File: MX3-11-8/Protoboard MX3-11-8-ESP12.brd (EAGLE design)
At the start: 74 x 99.4 mm, 638 parts, among them J1 DCJ0202, X3 RJ45

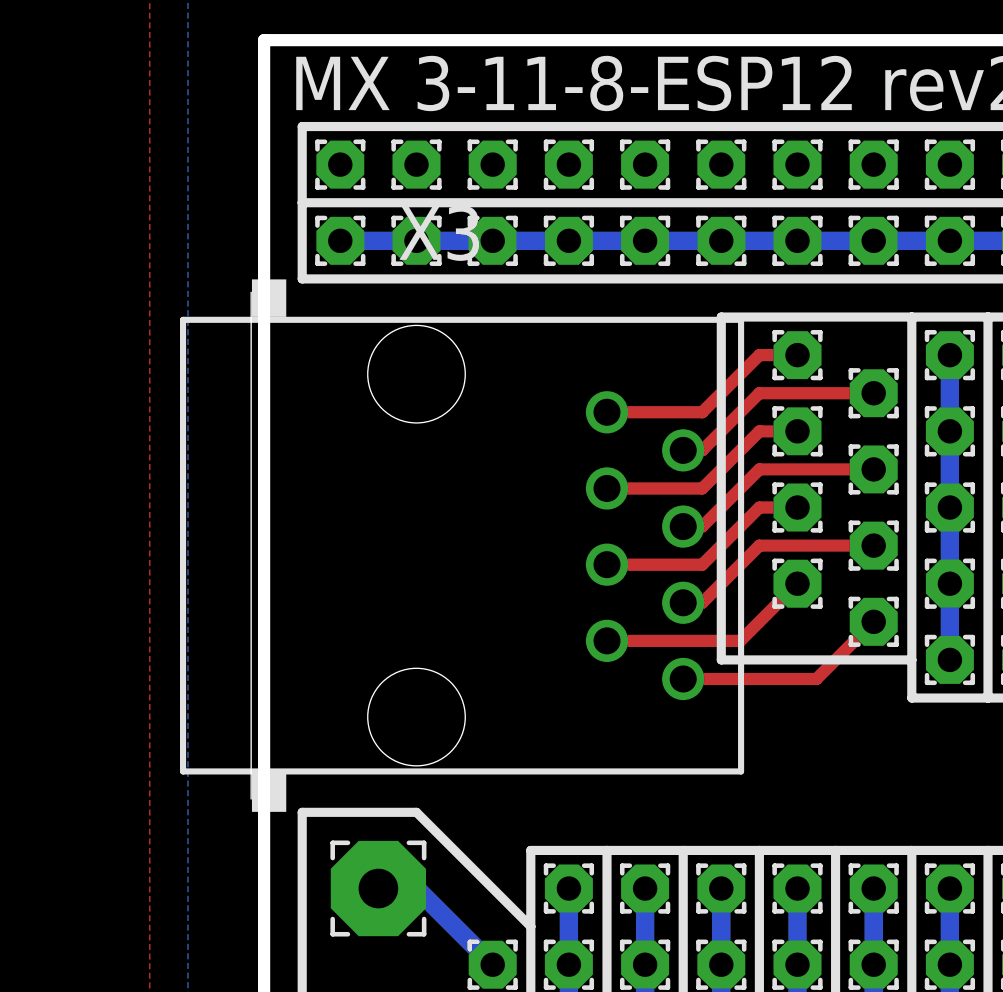
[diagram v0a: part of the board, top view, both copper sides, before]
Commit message: Moved RJ45
Moved RJ45 a bit into the board and created new Gerb files to factory
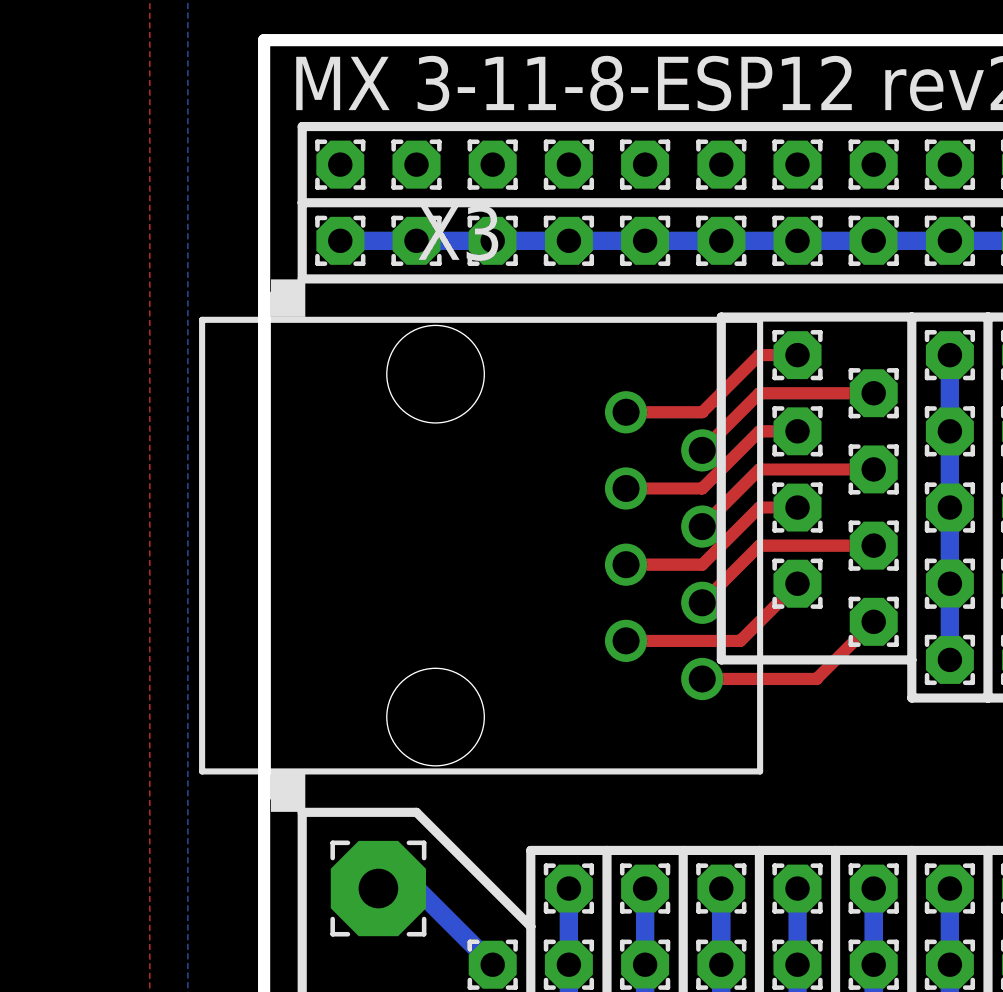
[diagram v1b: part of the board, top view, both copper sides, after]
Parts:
- moved X3 0.63 mm to (5.71, 82.5)
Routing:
- net N$89: track 7.14 -> 6.50 mm
- net N$84: track 7.14 -> 6.50 mm
- net N$65: track 7.14 -> 6.50 mm
- net N$64: track 7.14 -> 6.50 mm
- net N$63: track 7.14 -> 6.50 mm
- net N$104: track 7.14 -> 6.50 mm
- net N$103: track 7.14 -> 6.50 mm
- net N$102: track 7.14 -> 6.50 mm
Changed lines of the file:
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@@
 <?xml version="1.0" encoding="utf-8"?>
 <!DOCTYPE eagle SYSTEM "eagle.dtd">
-<eagle version="7.6.0">
+<eagle version="7.7.0">
 <drawing>
 <settings>
@@
 <attribute name="VALUE" x="25.4" y="55.21" size="0.0254" layer="27"/>
 </element>
-<element name="X3" library="con-tycoelectronics" package="RJ45-NO-SHIELD" value="RJ45" x="5.08" y="82.55" smashed="yes" rot="R270">
-<attribute name="MF" value="TYCO ELECTRONICS" x="5.08" y="82.55" size="1.778" layer="27" rot="R270" display="off"/>
-<attribute name="OC_NEWARK" value="52K4445" x="5.08" y="82.55" size="1.778" layer="27" rot="R270" display="off"/>
-<attribute name="OC_FARNELL" value="1279843" x="5.08" y="82.55" size="1.778" layer="27" rot="R270" display="off"/>
-<attribute name="MPN" value="RJ45-8L-B" x="5.08" y="82.55" size="1.778" layer="27" rot="R270" display="off"/>
-<attribute name="NAME" x="4.445" y="92.075" size="1.778" layer="25"/>
-<attribute name="VALUE" x="7.62" y="85.09" size="1.778" layer="27" rot="R270"/>
+<element name="X3" library="con-tycoelectronics" package="RJ45-NO-SHIELD" value="RJ45" x="5.715" y="82.55" smashed="yes" rot="R270">
+<attribute name="MF" value="TYCO ELECTRONICS" x="5.715" y="82.55" size="1.778" layer="27" rot="R270" display="off"/>
+<attribute name="OC_NEWARK" value="52K4445" x="5.715" y="82.55" size="1.778" layer="27" rot="R270" display="off"/>
+<attribute name="OC_FARNELL" value="1279843" x="5.715" y="82.55" size="1.778" layer="27" rot="R270" display="off"/>
+<attribute name="MPN" value="RJ45-8L-B" x="5.715" y="82.55" size="1.778" layer="27" rot="R270" display="off"/>
+<attribute name="NAME" x="5.08" y="92.075" size="1.778" layer="25"/>
+<attribute name="VALUE" x="8.255" y="85.09" size="1.778" layer="27" rot="R270"/>
 </element>
 <element name="1" library="wirepad" package="1,6/0,8" value="" x="20.32" y="80.01" smashed="yes">
@@
 <wire x1="17.78" y1="88.9" x2="16.51" y2="88.9" width="0.4064" layer="1"/>
 <wire x1="16.51" y1="88.9" x2="14.605" y2="86.995" width="0.4064" layer="1"/>
-<wire x1="14.605" y1="86.995" x2="11.43" y2="86.995" width="0.4064" layer="1"/>
+<wire x1="14.605" y1="86.995" x2="12.065" y2="86.995" width="0.4064" layer="1"/>
 </signal>
 <signal name="N$64">
 <contactref element="RJ-3" pad="1"/>
 <contactref element="X3" pad="2"/>
-<wire x1="13.97" y1="85.725" x2="14.605" y2="85.725" width="0.4064" layer="1"/>
 <wire x1="14.605" y1="85.725" x2="16.51" y2="87.63" width="0.4064" layer="1"/>
 <wire x1="16.51" y1="87.63" x2="20.32" y2="87.63" width="0.4064" layer="1"/>
@@
 <wire x1="17.78" y1="86.36" x2="16.51" y2="86.36" width="0.4064" layer="1"/>
 <wire x1="16.51" y1="86.36" x2="14.605" y2="84.455" width="0.4064" layer="1"/>
-<wire x1="14.605" y1="84.455" x2="11.43" y2="84.455" width="0.4064" layer="1"/>
+<wire x1="14.605" y1="84.455" x2="12.065" y2="84.455" width="0.4064" layer="1"/>
 </signal>
 <signal name="N$84">
 <contactref element="5" pad="1"/>
 <contactref element="X3" pad="4"/>
-<wire x1="13.97" y1="83.185" x2="14.605" y2="83.185" width="0.4064" layer="1"/>
 <wire x1="14.605" y1="83.185" x2="16.51" y2="85.09" width="0.4064" layer="1"/>
 <wire x1="16.51" y1="85.09" x2="20.32" y2="85.09" width="0.4064" layer="1"/>
@@
 <wire x1="17.78" y1="83.82" x2="16.51" y2="83.82" width="0.4064" layer="1"/>
 <wire x1="16.51" y1="83.82" x2="14.605" y2="81.915" width="0.4064" layer="1"/>
-<wire x1="14.605" y1="81.915" x2="11.43" y2="81.915" width="0.4064" layer="1"/>
+<wire x1="14.605" y1="81.915" x2="12.065" y2="81.915" width="0.4064" layer="1"/>
 </signal>
 <signal name="N$102">
 <contactref element="7" pad="1"/>
 <contactref element="X3" pad="6"/>
-<wire x1="13.97" y1="80.645" x2="14.605" y2="80.645" width="0.4064" layer="1"/>
 <wire x1="14.605" y1="80.645" x2="16.51" y2="82.55" width="0.4064" layer="1"/>
 <wire x1="16.51" y1="82.55" x2="20.32" y2="82.55" width="0.4064" layer="1"/>
@@
 <contactref element="8" pad="1"/>
 <contactref element="X3" pad="7"/>
-<wire x1="11.43" y1="79.375" x2="15.875" y2="79.375" width="0.4064" layer="1"/>
+<wire x1="12.065" y1="79.375" x2="15.875" y2="79.375" width="0.4064" layer="1"/>
 <wire x1="15.875" y1="79.375" x2="17.78" y2="81.28" width="0.4064" layer="1"/>
 </signal>
@@
 <contactref element="1" pad="1"/>
 <contactref element="X3" pad="8"/>
-<wire x1="13.97" y1="78.105" x2="18.415" y2="78.105" width="0.4064" layer="1"/>
+<wire x1="14.605" y1="78.105" x2="18.415" y2="78.105" width="0.4064" layer="1"/>
 <wire x1="18.415" y1="78.105" x2="20.32" y2="80.01" width="0.4064" layer="1"/>
 </signal>

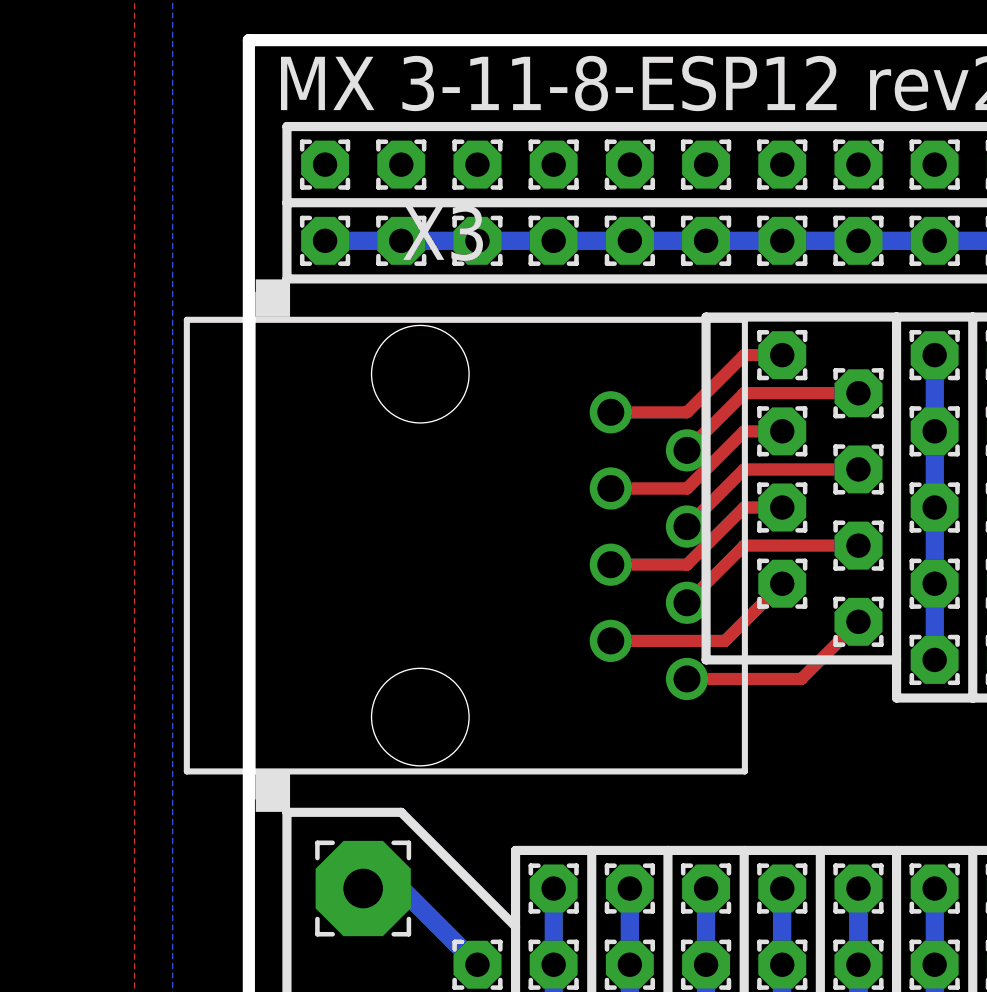
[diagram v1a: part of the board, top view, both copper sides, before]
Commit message: Moved RJ45 5mil to the left, to align it's outline to board outline
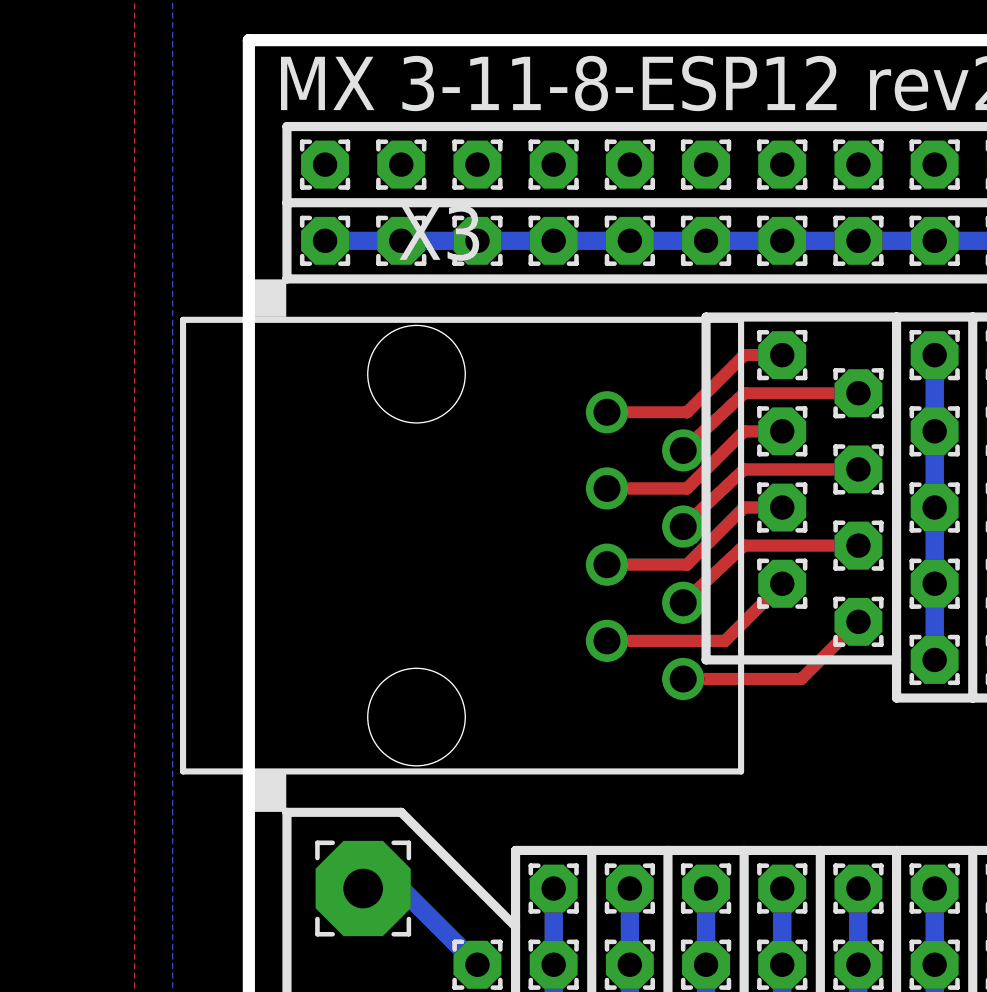
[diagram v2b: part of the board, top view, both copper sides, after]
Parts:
- moved X3 0.13 mm to (5.59, 82.5)
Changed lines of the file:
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@@
 <?xml version="1.0" encoding="utf-8"?>
 <!DOCTYPE eagle SYSTEM "eagle.dtd">
-<eagle version="7.7.0">
+<eagle version="7.6.0">
 <drawing>
 <settings>
@@
 <setting verticaltext="up"/>
 </settings>
-<grid distance="50" unitdist="mil" unit="mil" style="dots" multiple="1" display="yes" altdistance="25" altunitdist="mil" altunit="mil"/>
+<grid distance="50" unitdist="mil" unit="mil" style="dots" multiple="1" display="yes" altdistance="5" altunitdist="mil" altunit="mil"/>
 <layers>
 <layer number="1" name="Top" color="4" fill="1" visible="yes" active="yes"/>
@@
 <attribute name="VALUE" x="25.4" y="55.21" size="0.0254" layer="27"/>
 </element>
-<element name="X3" library="con-tycoelectronics" package="RJ45-NO-SHIELD" value="RJ45" x="5.715" y="82.55" smashed="yes" rot="R270">
-<attribute name="MF" value="TYCO ELECTRONICS" x="5.715" y="82.55" size="1.778" layer="27" rot="R270" display="off"/>
-<attribute name="OC_NEWARK" value="52K4445" x="5.715" y="82.55" size="1.778" layer="27" rot="R270" display="off"/>
-<attribute name="OC_FARNELL" value="1279843" x="5.715" y="82.55" size="1.778" layer="27" rot="R270" display="off"/>
-<attribute name="MPN" value="RJ45-8L-B" x="5.715" y="82.55" size="1.778" layer="27" rot="R270" display="off"/>
-<attribute name="NAME" x="5.08" y="92.075" size="1.778" layer="25"/>
-<attribute name="VALUE" x="8.255" y="85.09" size="1.778" layer="27" rot="R270"/>
+<element name="X3" library="con-tycoelectronics" package="RJ45-NO-SHIELD" value="RJ45" x="5.588" y="82.55" smashed="yes" rot="R270">
+<attribute name="MF" value="TYCO ELECTRONICS" x="5.588" y="82.55" size="1.778" layer="27" rot="R270" display="off"/>
+<attribute name="OC_NEWARK" value="52K4445" x="5.588" y="82.55" size="1.778" layer="27" rot="R270" display="off"/>
+<attribute name="OC_FARNELL" value="1279843" x="5.588" y="82.55" size="1.778" layer="27" rot="R270" display="off"/>
+<attribute name="MPN" value="RJ45-8L-B" x="5.588" y="82.55" size="1.778" layer="27" rot="R270" display="off"/>
+<attribute name="NAME" x="4.953" y="92.075" size="1.778" layer="25"/>
+<attribute name="VALUE" x="8.128" y="85.09" size="1.778" layer="27" rot="R270"/>
 </element>
 <element name="1" library="wirepad" package="1,6/0,8" value="" x="20.32" y="80.01" smashed="yes">
@@
 <wire x1="17.78" y1="88.9" x2="16.51" y2="88.9" width="0.4064" layer="1"/>
 <wire x1="16.51" y1="88.9" x2="14.605" y2="86.995" width="0.4064" layer="1"/>
-<wire x1="14.605" y1="86.995" x2="12.065" y2="86.995" width="0.4064" layer="1"/>
+<wire x1="14.605" y1="86.995" x2="11.938" y2="86.995" width="0.4064" layer="1"/>
 </signal>
 <signal name="N$64">
 <contactref element="RJ-3" pad="1"/>
 <contactref element="X3" pad="2"/>
-<wire x1="14.605" y1="85.725" x2="16.51" y2="87.63" width="0.4064" layer="1"/>
+<wire x1="14.478" y1="85.725" x2="16.51" y2="87.63" width="0.4064" layer="1"/>
 <wire x1="16.51" y1="87.63" x2="20.32" y2="87.63" width="0.4064" layer="1"/>
 </signal>
@@
 <wire x1="17.78" y1="86.36" x2="16.51" y2="86.36" width="0.4064" layer="1"/>
 <wire x1="16.51" y1="86.36" x2="14.605" y2="84.455" width="0.4064" layer="1"/>
-<wire x1="14.605" y1="84.455" x2="12.065" y2="84.455" width="0.4064" layer="1"/>
+<wire x1="14.605" y1="84.455" x2="11.938" y2="84.455" width="0.4064" layer="1"/>
 </signal>
 <signal name="N$84">
 <contactref element="5" pad="1"/>
 <contactref element="X3" pad="4"/>
-<wire x1="14.605" y1="83.185" x2="16.51" y2="85.09" width="0.4064" layer="1"/>
+<wire x1="14.478" y1="83.185" x2="16.51" y2="85.09" width="0.4064" layer="1"/>
 <wire x1="16.51" y1="85.09" x2="20.32" y2="85.09" width="0.4064" layer="1"/>
 </signal>
@@
 <wire x1="17.78" y1="83.82" x2="16.51" y2="83.82" width="0.4064" layer="1"/>
 <wire x1="16.51" y1="83.82" x2="14.605" y2="81.915" width="0.4064" layer="1"/>
-<wire x1="14.605" y1="81.915" x2="12.065" y2="81.915" width="0.4064" layer="1"/>
+<wire x1="14.605" y1="81.915" x2="11.938" y2="81.915" width="0.4064" layer="1"/>
 </signal>
 <signal name="N$102">
 <contactref element="7" pad="1"/>
 <contactref element="X3" pad="6"/>
-<wire x1="14.605" y1="80.645" x2="16.51" y2="82.55" width="0.4064" layer="1"/>
+<wire x1="14.478" y1="80.645" x2="16.51" y2="82.55" width="0.4064" layer="1"/>
 <wire x1="16.51" y1="82.55" x2="20.32" y2="82.55" width="0.4064" layer="1"/>
 </signal>
@@
 <contactref element="8" pad="1"/>
 <contactref element="X3" pad="7"/>
-<wire x1="12.065" y1="79.375" x2="15.875" y2="79.375" width="0.4064" layer="1"/>
+<wire x1="11.938" y1="79.375" x2="15.875" y2="79.375" width="0.4064" layer="1"/>
 <wire x1="15.875" y1="79.375" x2="17.78" y2="81.28" width="0.4064" layer="1"/>
 </signal>
@@
 <contactref element="1" pad="1"/>
 <contactref element="X3" pad="8"/>
-<wire x1="14.605" y1="78.105" x2="18.415" y2="78.105" width="0.4064" layer="1"/>
+<wire x1="14.478" y1="78.105" x2="18.415" y2="78.105" width="0.4064" layer="1"/>
 <wire x1="18.415" y1="78.105" x2="20.32" y2="80.01" width="0.4064" layer="1"/>
 </signal>
